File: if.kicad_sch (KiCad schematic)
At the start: 59 parts, among them U34 ADA4940-2, U35 ADA4940-2

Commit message: final corrections is done. Working!
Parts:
- R55, R56, R57, R58: value 550 -> 1k
- R59, R60, R61, R62: value 8.2k -> 20.5k
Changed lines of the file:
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@@
 			)
 		)
-		(property "Value" "8.2k"
+		(property "Value" "20.5k"
 			(at 99.06 27.94 90)
 			(effects
@@
 			)
 		)
-		(property "Value" "8.2k"
+		(property "Value" "20.5k"
 			(at 99.06 66.04 90)
 			(effects
@@
 			)
 		)
-		(property "Value" "550"
+		(property "Value" "1k"
 			(at 73.66 44.45 90)
 			(effects
@@
 			)
 		)
-		(property "Value" "550"
+		(property "Value" "1k"
 			(at 73.66 52.07 90)
 			(effects
@@
 			)
 		)
-		(property "Value" "8.2k"
+		(property "Value" "20.5k"
 			(at 93.98 109.22 90)
 			(effects
@@
 			)
 		)
-		(property "Value" "8.2k"
+		(property "Value" "20.5k"
 			(at 93.98 147.32 90)
 			(effects
@@
 			)
 		)
-		(property "Value" "550"
+		(property "Value" "1k"
 			(at 68.58 125.73 90)
 			(effects
@@
 			)
 		)
-		(property "Value" "550"
+		(property "Value" "1k"
 			(at 68.58 133.35 90)
 			(effects

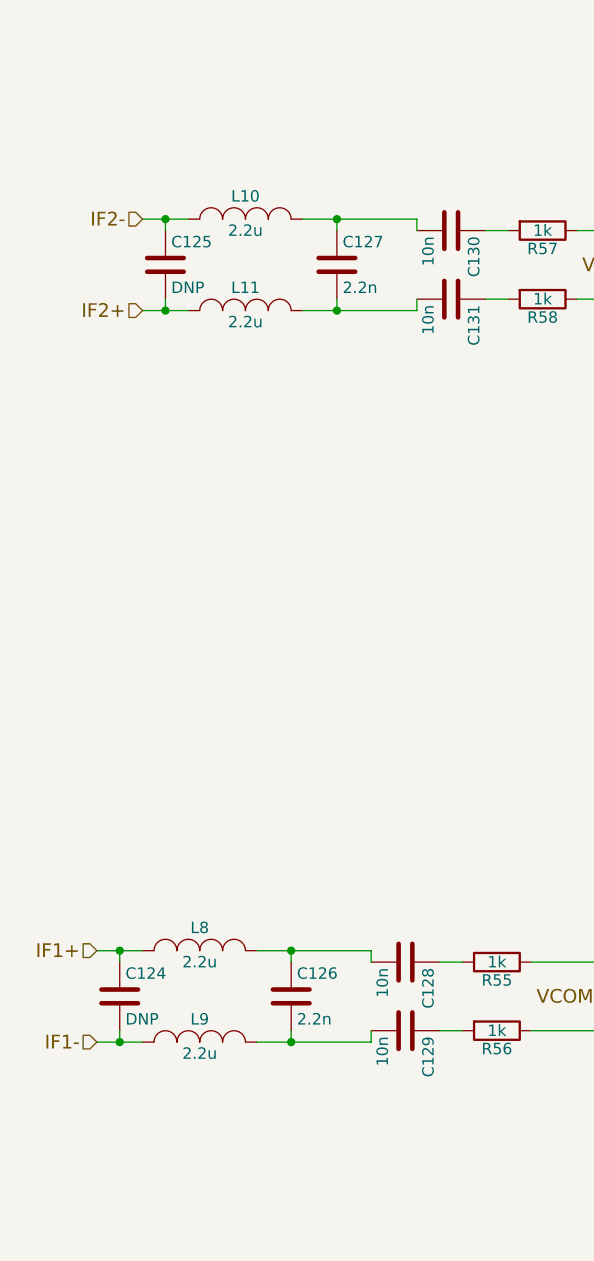
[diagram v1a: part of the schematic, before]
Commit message: Minor changes are done. Pcb is ready. Production file is added
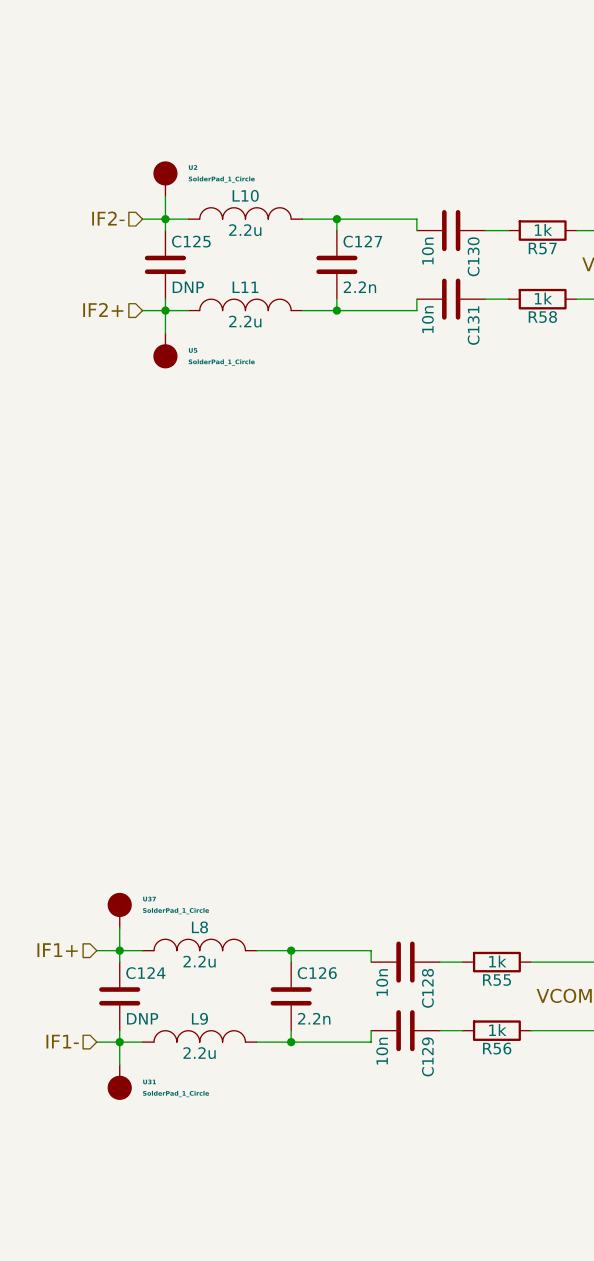
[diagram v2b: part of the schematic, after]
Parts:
- added U2, U31, U37, U5: SolderPad_1_Circle, Footprints:SolderPad_1_1.0mm_SMD_Circle, symbol SolderPad_1_Circle:SolderPad_1_Circle
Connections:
- net IF1+: now also U37.1
- net IF1-: now also U31.1
- net IF2+: now also U5.1
- net IF2-: now also U2.1

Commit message: final changes
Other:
- note added: "Second stage of the amplifier is not used. FPGA FIR Filter works perfectly. Can be removed."
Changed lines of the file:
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@@
 	(generator_version "9.0")
 	(paper "A4")
+	(text "Second stage of the amplifier is not used.\nFPGA FIR Filter works perfectly. \nCan be removed."
+		(exclude_from_sim no)
+		(at 210.312 89.154 0)
+		(effects
+			(font
+				(size 2.54 2.54)
+			)
+		)
+	)
 	(junction
 		(at 127 20.32)

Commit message: hardware changes
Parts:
- removed C140, C141, C142, C143, C144, C145, C146, C147, C148, C149: DNP, Footprints:SMD_0402, symbol fmcw3-rescue:C
- removed C150, C151: 100n, Footprints:SMD_0402, symbol fmcw3-rescue:C
- removed R63, R64, R65, R66, R67, R68, R74, R75, R76, R77, R78, R86: DNP, Footprints:SMD_0402, symbol fmcw3-rescue:R
- removed U35: ADA4940-2, fmcw3:VFQFN-24, symbol fmcw3:ADA4940-2
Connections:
- net OUT1+: now also R94.2; no longer R94.1
- net OUT2+: now also R89.2; no longer R89.1
- net at U34.18 (+OUT): now also R89.1; no longer R89.2
- net at U34.12 (+OUT): now also R94.1; no longer R94.2
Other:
- note added: "FPGA FIR Filter works perfectly. Second stage is removed"
- note removed: "Second stage of the amplifier is not used. FPGA FIR Filter works perfectly. Can be removed."
- moved on the sheet: C124, C125, C126, C127, C128, C129, C130, C131, C132, C133, C134, C135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
